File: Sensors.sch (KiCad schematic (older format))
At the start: 54 parts, among them CON1 CONSOLE, P1 CONN_02X20, P10 CBUS, P13 I2C1, P14 I2C1, P7 96B_SPI, U1 CJT1117-3.3, U2 XC6206, U3 FT230XS, U4 TXB0108PW, U5 TXS0108E, U6 PCA9306, U7 PCA9306

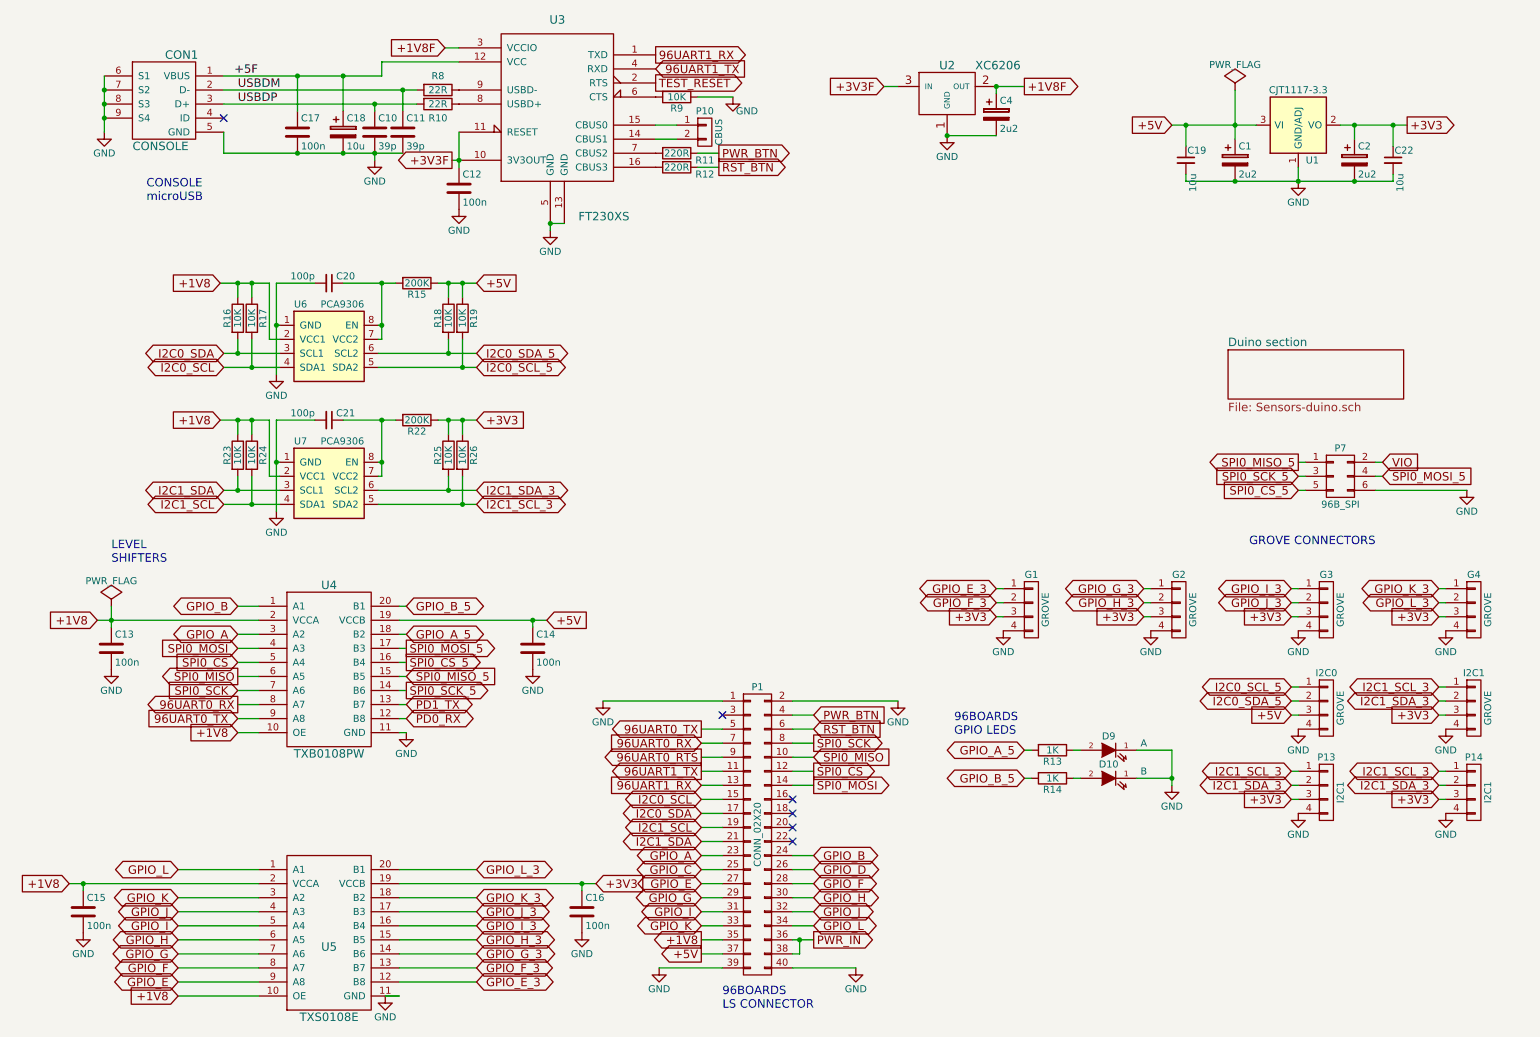
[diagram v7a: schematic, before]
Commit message: Change one of the Grove connectors to be GPIO
GPIO A & B are level shifted, but they weren't exposed anywhere other
than to drive a couple of LEDs. Repurpose one of the 3.3V I2C connectors
to be GPIO instead.

Signed-off-by: Grant Likely <grant.likely@linaro.org>
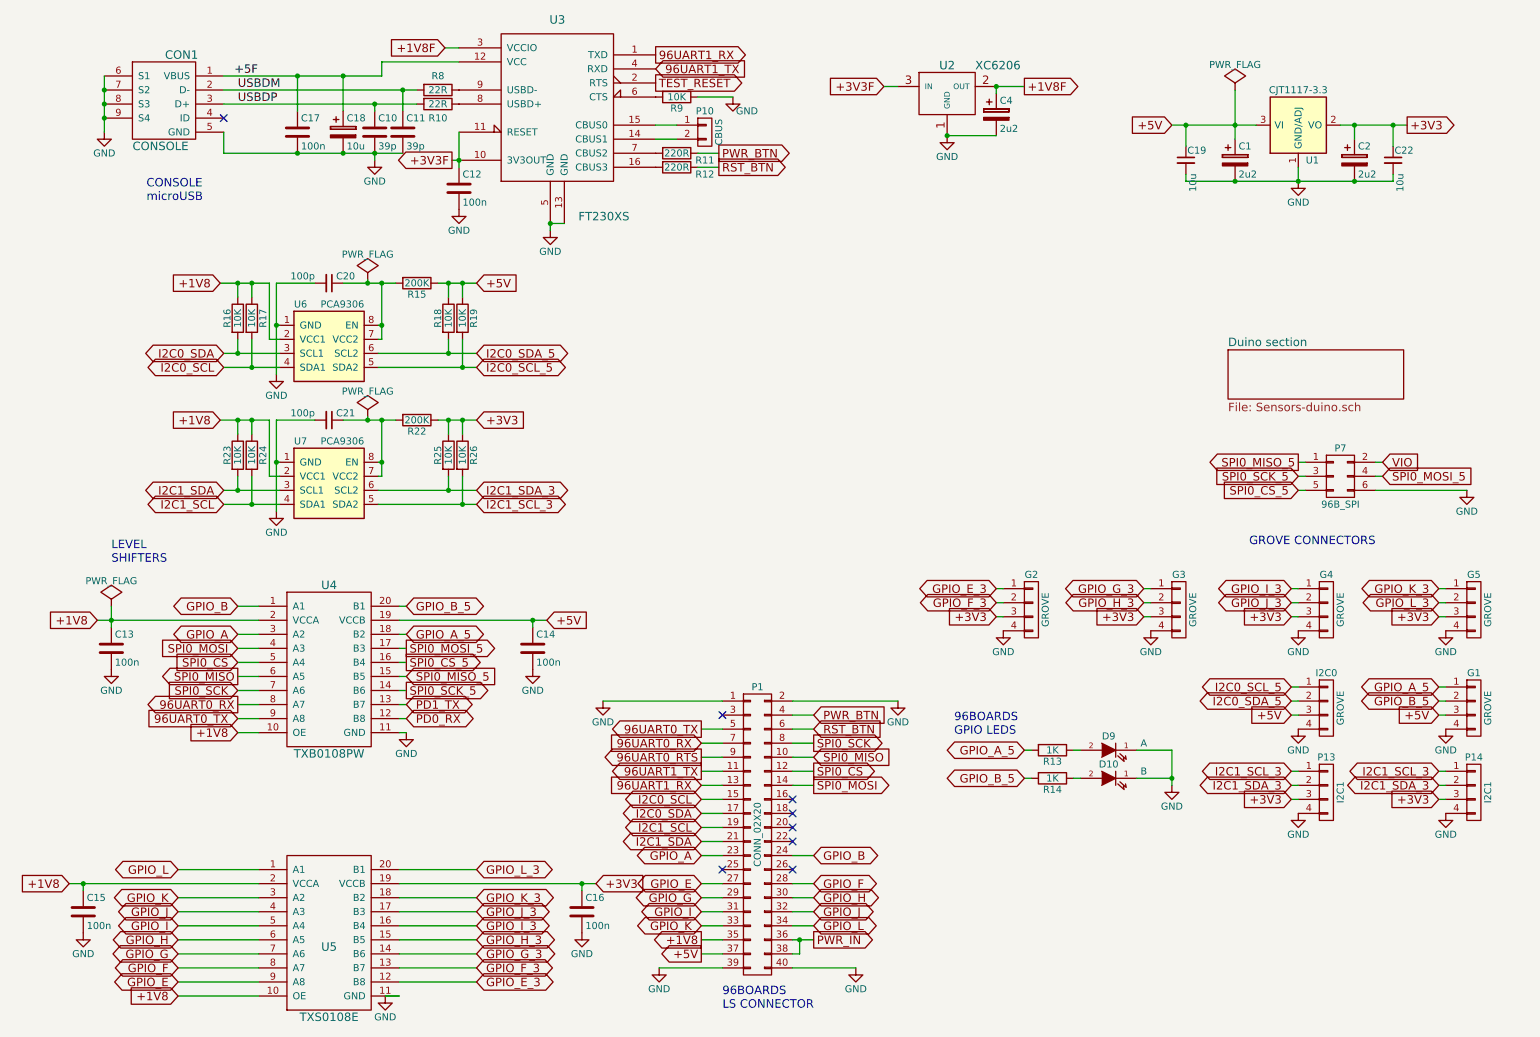
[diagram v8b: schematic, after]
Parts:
- renumbered I2C1 to G1, G1 to G2, G2 to G3, G3 to G4, G4 to G5
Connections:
- net +3V3: no longer G1.3 (P3)
- net +5V: now also G1.3 (P3)
- net GPIO_A_5: now also G1.1 (P1)
- net GPIO_B_5: now also G1.2 (P2)
- net I2C1_SCL_3: no longer G1.1 (P1)
- net I2C1_SDA_3: no longer G1.2 (P2)
- net GPIO_C: no longer names the net of P1.25 (P25)
- net GPIO_D: no longer names the net of P1.26 (P26)
- no-connect marks 6 -> 8
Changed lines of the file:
@@
 $EndComp
 $Comp
-L CONN_01X04 I2C1
+L CONN_01X04 G1
 U 1 1 55BC07A4
 P 10900 5550
-F 0 "I2C1" H 10900 5800 50  0000 C CNN
+F 0 "G1" H 10900 5800 50  0000 C CNN
 F 1 "GROVE" V 11000 5550 50  0000 C CNN
 F 2 "Sensors:Grove4P" H 10900 5550 60  0001 C CNN
@@
 $EndComp
 Text GLabel 10650 5600 0    60   Input ~ 0
-+3V3
++5V
 Text GLabel 9600 5600 0    60   Input ~ 0
 +5V
@@
 I2C0_SDA_5
 Text GLabel 10650 5400 0    60   BiDi ~ 0
-I2C1_SCL_3
+GPIO_A_5
 Text GLabel 10650 5500 0    60   BiDi ~ 0
-I2C1_SDA_3
+GPIO_B_5
 $Comp
 L TXS0108E U5
@@
 Text GLabel 5400 6600 0    60   BiDi ~ 0
 GPIO_A
-Text GLabel 5400 6700 0    60   BiDi ~ 0
-GPIO_C
 Text GLabel 6200 6600 2    60   BiDi ~ 0
 GPIO_B
-Text GLabel 6200 6700 2    60   BiDi ~ 0
-GPIO_D
 Text GLabel 7700 5850 0    60   BiDi ~ 0
 GPIO_A_5
@@
 $EndComp
 $Comp
-L CONN_01X04 G3
+L CONN_01X04 G4
 U 1 1 5616B627
 P 9850 4850
-F 0 "G3" H 9850 5100 50  0000 C CNN
+F 0 "G4" H 9850 5100 50  0000 C CNN
 F 1 "GROVE" V 9950 4850 50  0000 C CNN
 F 2 "Sensors:Grove4P" H 9850 4850 60  0001 C CNN
@@
 $EndComp
 $Comp
-L CONN_01X04 G2
+L CONN_01X04 G3
 U 1 1 55C534B2
 P 8800 4850
-F 0 "G2" H 8800 5100 50  0000 C CNN
+F 0 "G3" H 8800 5100 50  0000 C CNN
 F 1 "GROVE" V 8900 4850 50  0000 C CNN
 F 2 "Sensors:Grove4P" H 8800 4850 60  0001 C CNN
@@
 $EndComp
 $Comp
-L CONN_01X04 G1
+L CONN_01X04 G2
 U 1 1 561DB333
 P 7750 4850
-F 0 "G1" H 7750 5100 50  0000 C CNN
+F 0 "G2" H 7750 5100 50  0000 C CNN
 F 1 "GROVE" V 7850 4850 50  0000 C CNN
 F 2 "Sensors:Grove_SMD_Connector" H 7750 4850 60  0001 C CNN
@@
 $EndComp
 $Comp
-L CONN_01X04 G4
+L CONN_01X04 G5
 U 1 1 565A18B5
 P 10900 4850
-F 0 "G4" H 10900 5100 50  0000 C CNN
+F 0 "G5" H 10900 5100 50  0000 C CNN
 F 1 "GROVE" V 11000 4850 50  0000 C CNN
 F 2 "Sensors:Grove4P" H 10900 4850 60  0001 C CNN
@@
 Connection ~ 9650 1800
 Wire Wire Line
-	6050 6700 6200 6700
-Wire Wire Line
 	6050 6600 6200 6600
-Wire Wire Line
-	5400 6700 5550 6700
 Wire Wire Line
 	5400 6600 5550 6600
@@
 Text Label 2100 1250 0    60   ~ 0
 USBDP
+$Comp
+L PWR_FLAG #FLG032
+U 1 1 565B9F82
+P 3025 2500
+F 0 "#FLG032" H 3025 2595 50  0001 C CNN
+F 1 "PWR_FLAG" H 3025 2680 50  0000 C CNN
+F 2 "" H 3025 2500 60  0000 C CNN
+F 3 "" H 3025 2500 60  0000 C CNN
+	1    3025 2500
+	1    0    0    -1
+$EndComp
+Wire Wire Line
+	3025 2500 3025 2525
+Connection ~ 3025 2525
+$Comp
+L PWR_FLAG #FLG033
+U 1 1 565BA35B
+P 3025 3475
+F 0 "#FLG033" H 3025 3570 50  0001 C CNN
+F 1 "PWR_FLAG" H 3025 3655 50  0000 C CNN
+F 2 "" H 3025 3475 60  0000 C CNN
+F 3 "" H 3025 3475 60  0000 C CNN
+	1    3025 3475
+	1    0    0    -1
+$EndComp
+Wire Wire Line
+	3025 3475 3025 3500
+Connection ~ 3025 3500
+NoConn ~ 6050 6700
+NoConn ~ 5550 6700
 $EndSCHEMATC
